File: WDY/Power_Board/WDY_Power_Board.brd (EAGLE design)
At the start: 57.1 x 41.1 mm, 48 parts, among them J1 22-05-7028-02, J2 22-05-7028-02, U1 LT3686HDDPBF, U2 LT3686HDDPBF, X1 MSTBA2

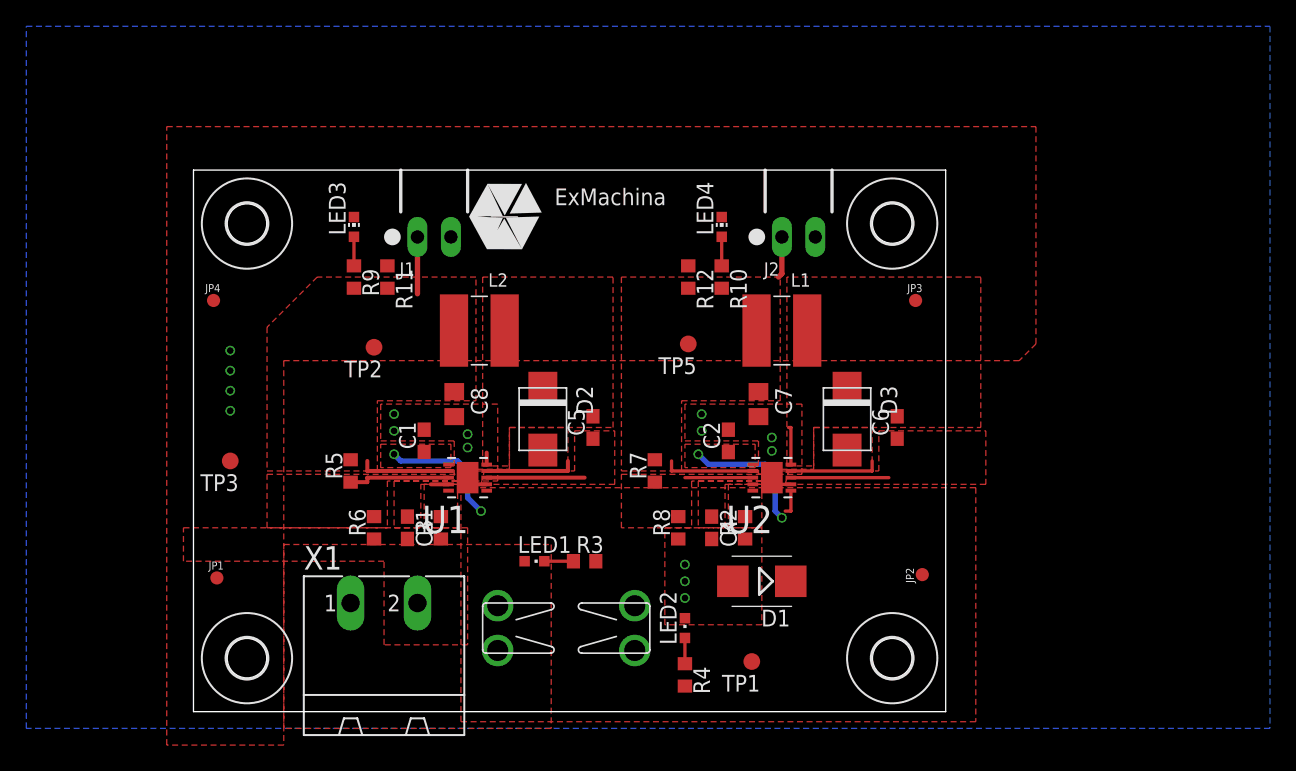
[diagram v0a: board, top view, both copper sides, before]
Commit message: Change layer top silkscreen
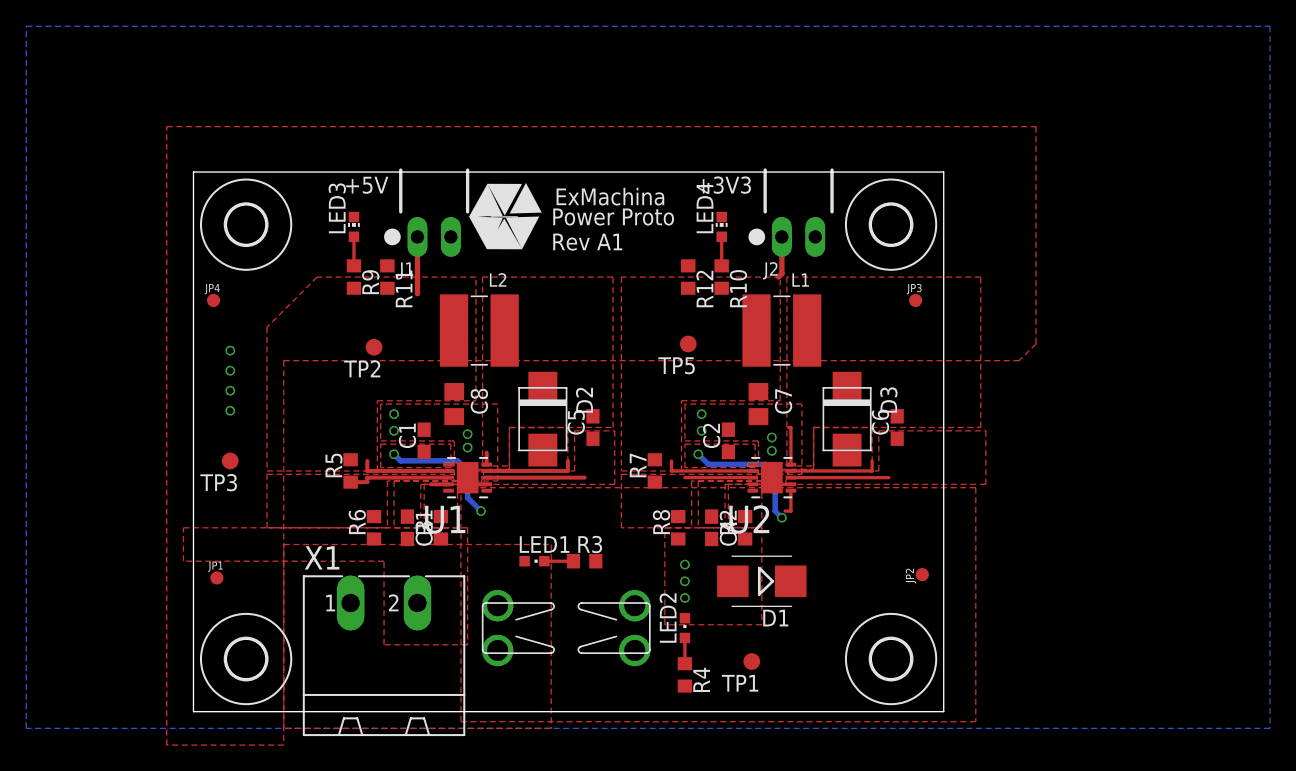
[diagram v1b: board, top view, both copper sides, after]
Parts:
- moved H2 0.12 mm to (53.0, 37.0)
- moved H1 0.11 mm to (53.0, 4.00)
- moved H3 0.11 mm to (4.00, 37.0)
- moved H4 0.09 mm to (4.00, 4.00)
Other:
- board size 57.1 x 41.1 mm -> 57 x 41 mm
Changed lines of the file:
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@@
 <setting verticaltext="up"/>
 </settings>
-<grid distance="0.05" unitdist="inch" unit="inch" style="lines" multiple="1" display="no" altdistance="0.01" altunitdist="inch" altunit="inch"/>
+<grid distance="0.05" unitdist="inch" unit="mm" style="lines" multiple="1" display="no" altdistance="0.01" altunitdist="inch" altunit="inch"/>
 <layers>
 <layer number="1" name="Top" color="4" fill="1" visible="yes" active="yes"/>
@@
 <board>
 <plain>
-<wire x1="0" y1="0" x2="57.15" y2="0" width="0" layer="20"/>
-<wire x1="57.15" y1="0" x2="57.15" y2="41.148" width="0" layer="20"/>
-<wire x1="57.15" y1="41.148" x2="0" y2="41.148" width="0" layer="20"/>
-<wire x1="0" y1="41.148" x2="0" y2="0" width="0" layer="20"/>
-<text x="27.178" y="35.052" size="1.27" layer="51" font="vector">Power Proto
+<wire x1="0" y1="0" x2="57" y2="0" width="0" layer="20"/>
+<wire x1="57" y1="0" x2="57" y2="41" width="0" layer="20"/>
+<wire x1="57" y1="41" x2="0" y2="41" width="0" layer="20"/>
+<wire x1="0" y1="41" x2="0" y2="0" width="0" layer="20"/>
+<text x="27.178" y="35.052" size="1.27" layer="21" font="vector">Power Proto
 Rev A1</text>
-<text x="11.43" y="39.37" size="1.27" layer="51" font="vector">+5V</text>
-<text x="38.1" y="39.37" size="1.27" layer="51" font="vector">+3V3</text>
+<text x="11.43" y="39.37" size="1.27" layer="21" font="vector">+5V</text>
+<text x="38.1" y="39.37" size="1.27" layer="21" font="vector">+3V3</text>
 </plain>
 <attributes>
@@
 <attribute name="MPN" value="" x="1.524" y="31.242" size="1.778" layer="27" display="off"/>
 </element>
-<element name="H1" library="holes" package="3,0" value="MOUNT-HOLE3.0" x="53.086" y="4.064">
-<attribute name="OC_NEWARK" value="unknown" x="53.086" y="4.064" size="1.778" layer="27" display="off"/>
-<attribute name="MF" value="" x="53.086" y="4.064" size="1.778" layer="27" display="off"/>
-<attribute name="MPN" value="" x="53.086" y="4.064" size="1.778" layer="27" display="off"/>
-</element>
-<element name="H2" library="holes" package="3,0" value="MOUNT-HOLE3.0" x="53.086" y="37.084">
-<attribute name="OC_NEWARK" value="unknown" x="53.086" y="37.084" size="1.778" layer="27" display="off"/>
-<attribute name="MF" value="" x="53.086" y="37.084" size="1.778" layer="27" display="off"/>
-<attribute name="MPN" value="" x="53.086" y="37.084" size="1.778" layer="27" display="off"/>
-</element>
-<element name="H3" library="holes" package="3,0" value="MOUNT-HOLE3.0" x="4.064" y="37.084">
-<attribute name="OC_NEWARK" value="unknown" x="4.064" y="37.084" size="1.778" layer="27" display="off"/>
-<attribute name="MF" value="" x="4.064" y="37.084" size="1.778" layer="27" display="off"/>
-<attribute name="MPN" value="" x="4.064" y="37.084" size="1.778" layer="27" display="off"/>
-</element>
-<element name="H4" library="holes" package="3,0" value="MOUNT-HOLE3.0" x="4.064" y="4.064">
-<attribute name="OC_NEWARK" value="unknown" x="4.064" y="4.064" size="1.778" layer="27" display="off"/>
-<attribute name="MF" value="" x="4.064" y="4.064" size="1.778" layer="27" display="off"/>
-<attribute name="MPN" value="" x="4.064" y="4.064" size="1.778" layer="27" display="off"/>
+<element name="H1" library="holes" package="3,0" value="MOUNT-HOLE3.0" x="53" y="4">
+<attribute name="OC_NEWARK" value="unknown" x="53" y="4" size="1.778" layer="27" display="off"/>
+<attribute name="MF" value="" x="53" y="4" size="1.778" layer="27" display="off"/>
+<attribute name="MPN" value="" x="53" y="4" size="1.778" layer="27" display="off"/>
+</element>
+<element name="H2" library="holes" package="3,0" value="MOUNT-HOLE3.0" x="53" y="37">
+<attribute name="OC_NEWARK" value="unknown" x="53" y="37" size="1.778" layer="27" display="off"/>
+<attribute name="MF" value="" x="53" y="37" size="1.778" layer="27" display="off"/>
+<attribute name="MPN" value="" x="53" y="37" size="1.778" layer="27" display="off"/>
+</element>
+<element name="H3" library="holes" package="3,0" value="MOUNT-HOLE3.0" x="4" y="37">
+<attribute name="OC_NEWARK" value="unknown" x="4" y="37" size="1.778" layer="27" display="off"/>
+<attribute name="MF" value="" x="4" y="37" size="1.778" layer="27" display="off"/>
+<attribute name="MPN" value="" x="4" y="37" size="1.778" layer="27" display="off"/>
+</element>
+<element name="H4" library="holes" package="3,0" value="MOUNT-HOLE3.0" x="4" y="4">
+<attribute name="OC_NEWARK" value="unknown" x="4" y="4" size="1.778" layer="27" display="off"/>
+<attribute name="MF" value="" x="4" y="4" size="1.778" layer="27" display="off"/>
+<attribute name="MPN" value="" x="4" y="4" size="1.778" layer="27" display="off"/>
 </element>
 <element name="J1" library="con-molex" package="7395-02" value="22-05-7028-02" x="18.288" y="36.068" rot="R180">

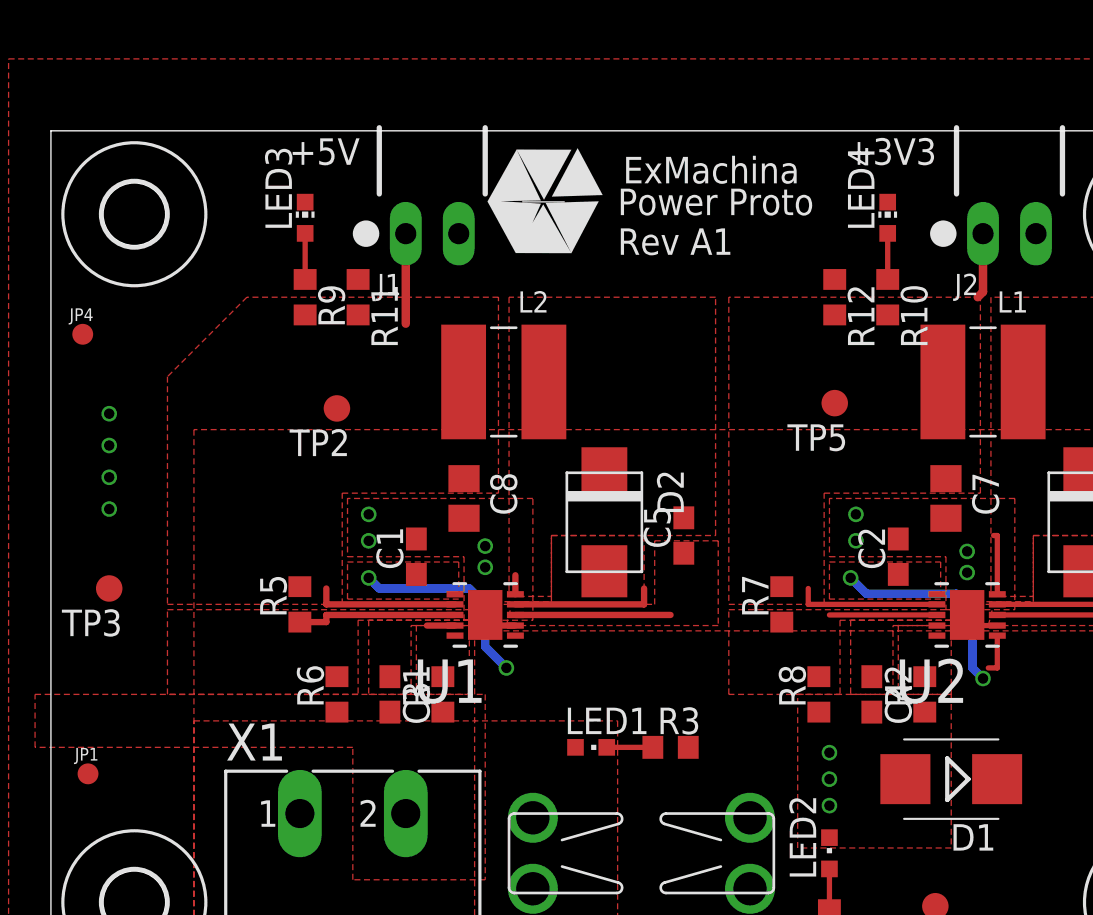
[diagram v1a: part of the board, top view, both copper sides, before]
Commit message: Re-generated gerber files for Power Board
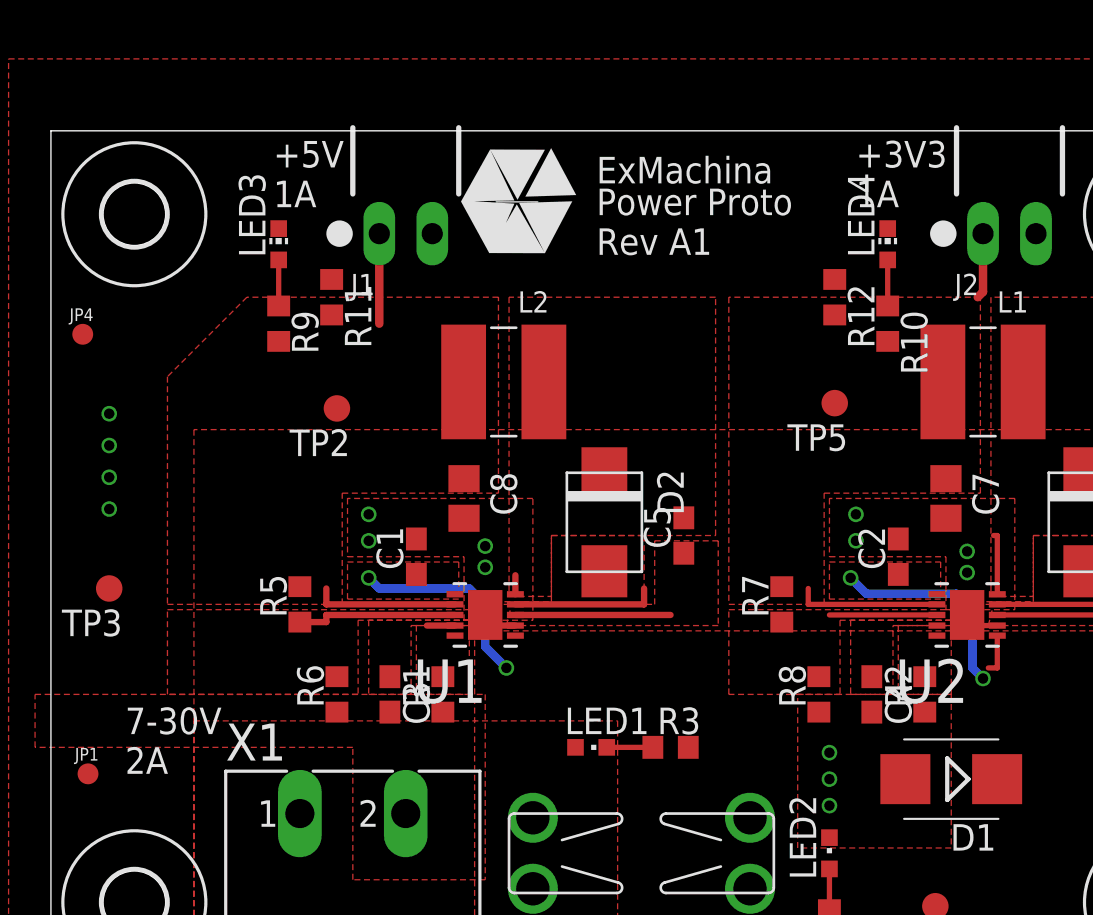
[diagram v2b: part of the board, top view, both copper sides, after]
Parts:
- moved R9 1.80 mm to (10.9, 31.8)
- moved LED3 1.80 mm to (10.9, 35.6)
- moved R10 1.27 mm to (40.1, 31.8)
- moved J1 1.27 mm to (17.0, 36.1)
- moved R11 1.27 mm to (13.5, 33.0)
- moved U$1 1.27 mm to (22.4, 37.6)
- moved LED4 1.27 mm to (40.1, 35.6)
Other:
- board text added: "+3V3 1A"
- board text added: "+5V 1A"
- board text added: "7-30V 2A"
- board text removed: "+3V3"
- board text removed: "+5V"
